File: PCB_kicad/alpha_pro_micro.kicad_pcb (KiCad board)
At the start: 2 copper layers, 192.9 x 59.5 mm, 72 parts, among them J1 Conn_01x03, J2 Conn_01x01_Female, J3 Conn_01x01_Female, J4 Conn_01x01_Female, J5 Conn_01x01_Female, J6 Conn_01x01_Female, J7 Conn_01x01_Female, J8 Conn_01x01_Female, J9 Conn_01x01_Female, K1 KEYSW, K10 KEYSW, K11 KEYSW, K12 KEYSW, K13 KEYSW, K14 KEYSW, K15 KEYSW, K16 KEYSW, K17 KEYSW, K18 KEYSW, K19 KEYSW, K2 KEYSW, K20 KEYSW, K21 KEYSW, K22 KEYSW, K23 KEYSW, K24 KEYSW, K25 KEYSW, K26 KEYSW, K27 KEYSW, K28 KEYSW, K3 KEYSW, K4 KEYSW, K5 KEYSW, K6 KEYSW, K7 KEYSW, K8 KEYSW, K9 KEYSW, SW1 SW_Push, U1 ProMicro

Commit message: Alpha v2.0 released!
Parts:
- K1, K10, K11, K12, K13, K14, K15, K16, K17, K18, K19, K2, K20, K21, K22, K23, K24, K26, K27, K28, K3, K4, K5, K6, K7, K8, K9: footprint MX_Alps_Hybrid:MX-1U-NoLED -> keebio-parts:MX-Alps-Choc-1U-NoLED
- K25: footprint MX_Alps_Hybrid:MX-2U-ReversedStabilizers-NoLED -> keebio-parts:MX-Alps-Choc-2U-StabFlip
- moved SW1 1.74 mm to (144.0, 102.5), turned to 180 degrees
- moved D28 1.52 mm to (237.1, 154.5)
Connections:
- K1 pad 1: /col0 -> Net-(D1-Pad2)
- K1 pad 2: Net-(D1-Pad2) -> /col0
- K10 pad 1: /col9 -> Net-(D10-Pad2)
- K10 pad 2: Net-(D10-Pad2) -> /col9
- K11 pad 1: /col0 -> Net-(D11-Pad2)
- K11 pad 2: Net-(D11-Pad2) -> /col0
- K12 pad 1: /col1 -> Net-(D12-Pad2)
- K12 pad 2: Net-(D12-Pad2) -> /col1
- K13 pad 1: /col2 -> Net-(D13-Pad2)
- K13 pad 2: Net-(D13-Pad2) -> /col2
- K14 pad 1: /col3 -> Net-(D14-Pad2)
- K14 pad 2: Net-(D14-Pad2) -> /col3
- K15 pad 1: /col4 -> Net-(D15-Pad2)
- K15 pad 2: Net-(D15-Pad2) -> /col4
- K16 pad 1: /col5 -> Net-(D16-Pad2)
- K16 pad 2: Net-(D16-Pad2) -> /col5
- K17 pad 1: /col6 -> Net-(D17-Pad2)
- K17 pad 2: Net-(D17-Pad2) -> /col6
- K18 pad 1: /col7 -> Net-(D18-Pad2)
- K18 pad 2: Net-(D18-Pad2) -> /col7
- K19 pad 1: /col8 -> Net-(D19-Pad2)
- K19 pad 2: Net-(D19-Pad2) -> /col8
- K2 pad 1: /col1 -> Net-(D2-Pad2)
- K2 pad 2: Net-(D2-Pad2) -> /col1
- K20 pad 1: /col9 -> Net-(D20-Pad2)
- K20 pad 2: Net-(D20-Pad2) -> /col9
- K21 pad 1: /col0 -> Net-(D21-Pad2)
- K21 pad 2: Net-(D21-Pad2) -> /col0
- K22 pad 1: /col1 -> Net-(D22-Pad2)
- K22 pad 2: Net-(D22-Pad2) -> /col1
- K23 pad 1: /col2 -> Net-(D23-Pad2)
- K23 pad 2: Net-(D23-Pad2) -> /col2
- K24 pad 1: /col3 -> Net-(D24-Pad2)
- K24 pad 2: Net-(D24-Pad2) -> /col3
- K26 pad 1: /col7 -> Net-(D26-Pad2)
- K26 pad 2: Net-(D26-Pad2) -> /col7
- K27 pad 1: /col8 -> Net-(D27-Pad2)
- K27 pad 2: Net-(D27-Pad2) -> /col8
- K28 pad 1: /col9 -> Net-(D28-Pad2)
- K28 pad 2: Net-(D28-Pad2) -> /col9
- K3 pad 1: /col2 -> Net-(D3-Pad2)
- K3 pad 2: Net-(D3-Pad2) -> /col2
- K4 pad 1: /col3 -> Net-(D4-Pad2)
- K4 pad 2: Net-(D4-Pad2) -> /col3
- K5 pad 1: /col4 -> Net-(D5-Pad2)
- K5 pad 2: Net-(D5-Pad2) -> /col4
- K6 pad 1: /col5 -> Net-(D6-Pad2)
- K6 pad 2: Net-(D6-Pad2) -> /col5
- K7 pad 1: /col6 -> Net-(D7-Pad2)
- K7 pad 2: Net-(D7-Pad2) -> /col6
- K8 pad 1: /col7 -> Net-(D8-Pad2)
- K8 pad 2: Net-(D8-Pad2) -> /col7
- K9 pad 1: /col8 -> Net-(D9-Pad2)
- K9 pad 2: Net-(D9-Pad2) -> /col8
- U1 pad 1: (no net) -> Net-(U1-Pad1)
- U1 pad 2: (no net) -> Net-(U1-Pad2)
- U1 pad 24: (no net) -> Net-(U1-Pad24)
- U1 pad 6: (no net) -> Net-(U1-Pad6)
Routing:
- net /col_tmo: track 268.5 -> 278.2 mm
- net /col3: track 50.2 -> 58.9 mm
- net /col2: track 47.2 -> 55.1 mm
- net /col5: track 90.2 -> 97.7 mm
- net /row1: track 204.6 -> 210.6 mm
- net /col6: track 92.7 -> 98.1 mm
- net /col0: track 76.6 -> 81.5 mm
- net Net-(D28-Pad2): track 9.52 -> 14.3 mm
- net /col7: track 133.9 -> 138.6 mm
- net /col8: track 153.7 -> 158.2 mm
- net RST: track 25.8 -> 21.6 mm
- net /row2: track 200.9 -> 204.4 mm
- net /col4: track 55.8 -> 58.9 mm
- net Net-(D10-Pad2): track 15.2 -> 18.2 mm
- net /col9: track 171.2 -> 174.2 mm
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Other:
- board text added: "v2.0"
- board text removed: "v1.2"

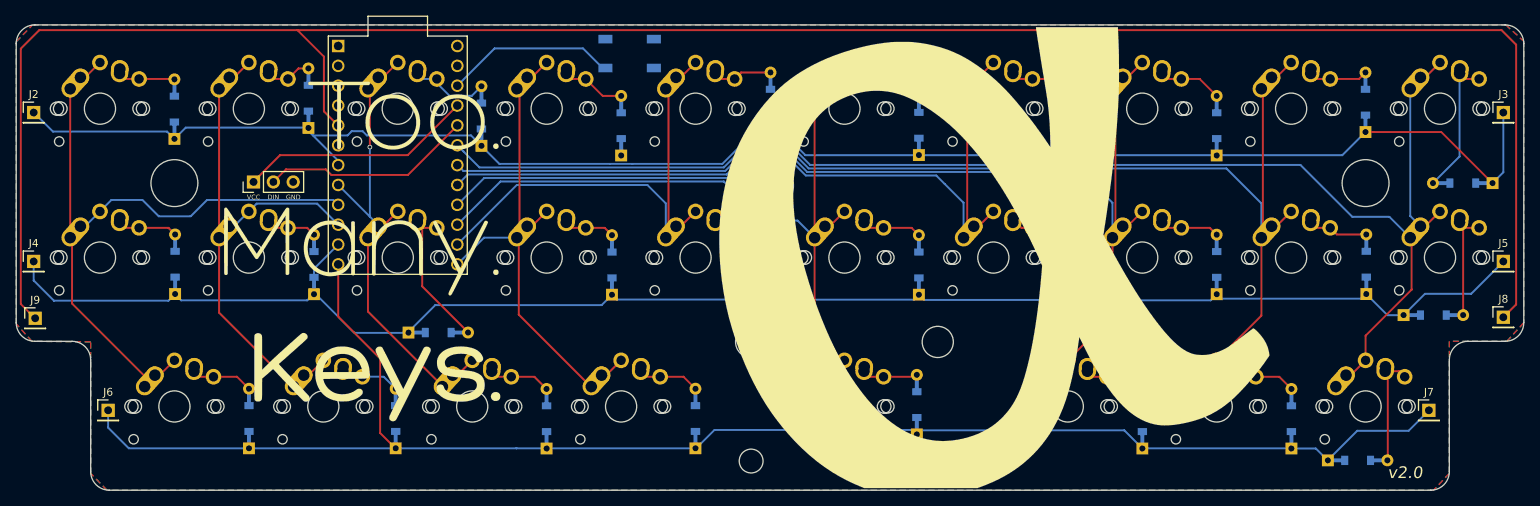
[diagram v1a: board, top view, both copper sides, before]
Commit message: v2.1 released: fixed disconnected D4
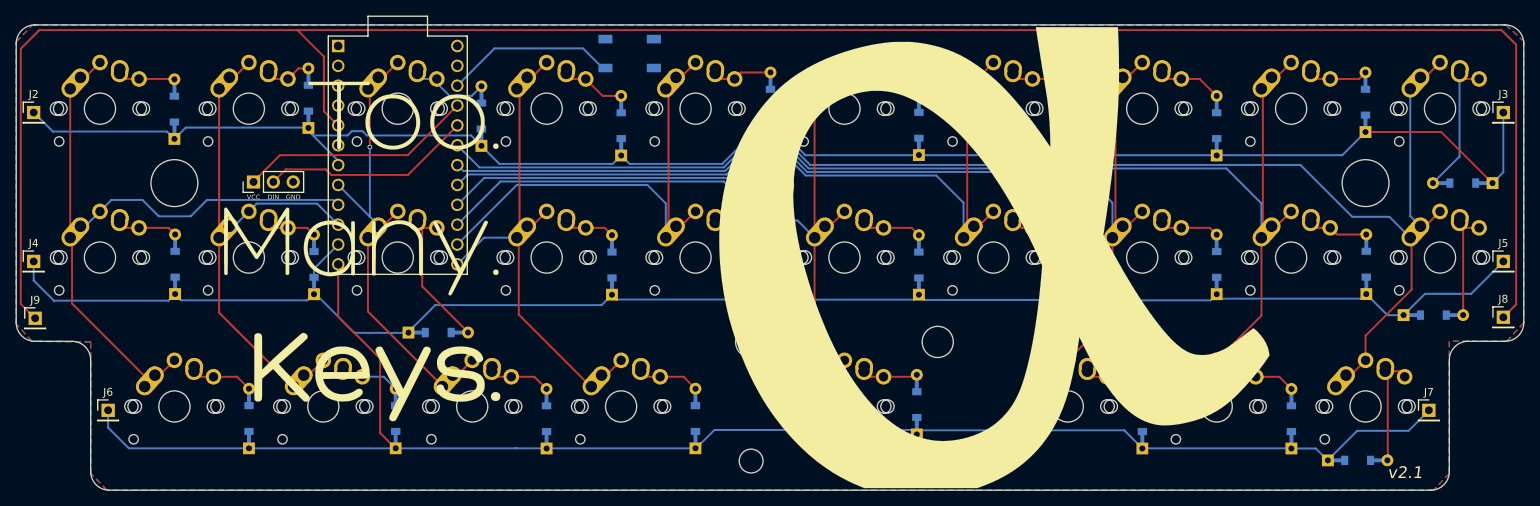
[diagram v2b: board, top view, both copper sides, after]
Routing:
- net /row0: track 211.5 -> 212.4 mm
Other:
- board text added: "v2.1"
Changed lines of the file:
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@@
     (thickness 1.6)
     (drawings 24)
-    (tracks 376)
+    (tracks 377)
     (zones 0)
     (modules 72)
@@
     (effects (font (size 1.5 1.5) (thickness 0.3) italic) (justify mirror))
   )
-  (gr_text v2.0 (at 243.179997 156.102844) (layer F.SilkS)
+  (gr_text v2.1 (at 243.179997 156.102844) (layer F.SilkS)
     (effects (font (size 1.5 1.5) (thickness 0.3) italic))
   )
@@
   (segment (start 161.925 112.514063) (end 162.720337 113.3094) (width 0.25) (layer B.Cu) (net 1))
   (segment (start 162.720337 113.3094) (end 164.267441 113.3094) (width 0.25) (layer B.Cu) (net 1))
-  (segment (start 161.114535 113.403506) (end 161.701895 112.816146) (width 0.25) (layer B.Cu) (net 1))
-  (segment (start 159.031251 113.403506) (end 161.114535 113.403506) (width 0.25) (layer B.Cu) (net 1))
-  (segment (start 155.827923 116.606835) (end 159.031251 113.403506) (width 0.25) (layer B.Cu) (net 1))
-  (segment (start 125.000941 114.307541) (end 127.300236 116.606836) (width 0.25) (layer B.Cu) (net 1))
   (segment (start 141.461133 116.606836) (end 141.461136 116.606833) (width 0.25) (layer B.Cu) (net 1))
-  (segment (start 141.461136 116.606833) (end 144.288864 116.606833) (width 0.25) (layer B.Cu) (net 1))
-  (segment (start 127.300236 116.606836) (end 141.461133 116.606836) (width 0.25) (layer B.Cu) (net 1))
   (segment (start 144.288864 116.606833) (end 144.288866 116.606835) (width 0.25) (layer B.Cu) (net 1))
-  (segment (start 144.288866 116.606835) (end 155.827923 116.606835) (width 0.25) (layer B.Cu) (net 1))
   (segment (start 239.124697 112.529144) (end 238.112697 112.529144) (width 0.25) (layer F.Cu) (net 1))
   (segment (start 247.809544 112.529144) (end 239.124697 112.529144) (width 0.25) (layer F.Cu) (net 1))
   (segment (start 254.343002 119.062602) (end 247.809544 112.529144) (width 0.25) (layer F.Cu) (net 1))
+  (segment (start 161.114535 113.403506) (end 161.701895 112.816146) (width 0.25) (layer B.Cu) (net 1))
+  (segment (start 159.031251 113.403506) (end 161.114535 113.403506) (width 0.25) (layer B.Cu) (net 1))
+  (segment (start 155.827923 116.606835) (end 159.031251 113.403506) (width 0.25) (layer B.Cu) (net 1))
+  (segment (start 142.888097 115.526344) (end 143.968588 116.606835) (width 0.25) (layer B.Cu) (net 1))
+  (segment (start 143.968588 116.606835) (end 155.827923 116.606835) (width 0.25) (layer B.Cu) (net 1))
+  (segment (start 127.300236 116.606836) (end 125.000941 114.307541) (width 0.25) (layer B.Cu) (net 1))
+  (segment (start 142.888097 115.526344) (end 141.807605 116.606836) (width 0.25) (layer B.Cu) (net 1))
+  (segment (start 141.807605 116.606836) (end 127.300236 116.606836) (width 0.25) (layer B.Cu) (net 1))
   (segment (start 78.7 105.0375) (end 78.84375 105.0375) (width 0.25) (layer B.Cu) (net 2) (status 30))
   (segment (start 79.4 105.7375) (end 81.2 105.7375) (width 0.25) (layer F.Cu) (net 2))

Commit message: tiny fix
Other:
- board text removed: "v2.0"
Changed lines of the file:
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@@
     (effects (font (size 0.6 0.6) (thickness 0.15)))
   )
-  (gr_text v2.0 (at 83.391137 154.393424) (layer B.SilkS)
+  (gr_text v2.1 (at 83.391137 154.393424) (layer B.SilkS)
     (effects (font (size 1.5 1.5) (thickness 0.3) italic) (justify mirror))
   )
